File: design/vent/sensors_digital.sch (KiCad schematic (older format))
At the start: 17 parts, among them J12 TEST_1P, J13 TEST_1P, Q1 DMG2302UK, Q2 DMG2302UK, U10 MS5607-02BA03, U6 LP2980AIM5-3.0, U7 LSM6DS3HTR, U8 BMG250, U9 LSM6DS3HTR

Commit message: Add connector part numbers to schematic
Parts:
- C12, C13, C16, C17: footprint Capacitors_SMD:C_0603_HandSoldering -> Capacitors_SMD:C_0805_HandSoldering
- J12, J13: footprint (none) -> TestPoint:TestPoint_Pad_D2.0mm
- Q1, Q2: footprint (none) -> TO_SOT_Packages_SMD:SOT-23_Handsoldering
- R13, R14: footprint (none) -> Resistors_SMD:R_0805_HandSoldering
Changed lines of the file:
@@
 $EndComp
 $Comp
-L GND #PWR61
+L GND #PWR049
 U 1 1 5AE13B89
 P 9100 3150
-F 0 "#PWR61" H 9100 2900 50  0001 C CNN
+F 0 "#PWR049" H 9100 2900 50  0001 C CNN
 F 1 "GND" H 9100 3000 50  0000 C CNN
 F 2 "" H 9100 3150 50  0001 C CNN
@@
 NoConn ~ 9300 1850
 $Comp
-L +3.0V #PWR49
+L +3.0V #PWR050
 U 1 1 5AE13B91
 P 9200 1550
-F 0 "#PWR49" H 9200 1400 50  0001 C CNN
+F 0 "#PWR050" H 9200 1400 50  0001 C CNN
 F 1 "+3.0V" H 9200 1690 50  0000 C CNN
 F 2 "" H 9200 1550 50  0001 C CNN
@@
 F 0 "C12" V 9500 1700 50  0000 L CNN
 F 1 "100nF" V 9500 1350 50  0000 L CNN
-F 2 "Capacitors_SMD:C_0603_HandSoldering" H 9488 1500 50  0001 C CNN
+F 2 "Capacitors_SMD:C_0805_HandSoldering" H 9488 1500 50  0001 C CNN
 F 3 "" H 9450 1650 50  0001 C CNN
 	1    9450 1650
@@
 $EndComp
 $Comp
-L GND #PWR50
+L GND #PWR051
 U 1 1 5AE13B9E
 P 9600 1650
-F 0 "#PWR50" H 9600 1400 50  0001 C CNN
+F 0 "#PWR051" H 9600 1400 50  0001 C CNN
 F 1 "GND" H 9600 1500 50  0000 C CNN
 F 2 "" H 9600 1650 50  0001 C CNN
@@
 $EndComp
 $Comp
-L GND #PWR60
+L GND #PWR052
 U 1 1 5AE13BA4
 P 9950 2800
-F 0 "#PWR60" H 9950 2550 50  0001 C CNN
+F 0 "#PWR052" H 9950 2550 50  0001 C CNN
 F 1 "GND" H 9950 2650 50  0000 C CNN
 F 2 "" H 9950 2800 50  0001 C CNN
@@
 F 0 "C17" H 7050 5200 50  0000 L CNN
 F 1 "100nF" H 6900 5000 50  0000 L CNN
-F 2 "Capacitors_SMD:C_0603_HandSoldering" H 7188 4950 50  0001 C CNN
+F 2 "Capacitors_SMD:C_0805_HandSoldering" H 7188 4950 50  0001 C CNN
 F 3 "" H 7150 5100 50  0001 C CNN
 	1    7150 5100
@@
 $EndComp
 $Comp
-L +3.0V #PWR69
+L +3.0V #PWR053
 U 1 1 5AE13BCB
 P 7150 4700
-F 0 "#PWR69" H 7150 4550 50  0001 C CNN
+F 0 "#PWR053" H 7150 4550 50  0001 C CNN
 F 1 "+3.0V" H 7150 4840 50  0000 C CNN
 F 2 "" H 7150 4700 50  0001 C CNN
@@
 $EndComp
 $Comp
-L GND #PWR72
+L GND #PWR054
 U 1 1 5AE13BD1
 P 7150 5250
-F 0 "#PWR72" H 7150 5000 50  0001 C CNN
+F 0 "#PWR054" H 7150 5000 50  0001 C CNN
 F 1 "GND" H 7150 5100 50  0000 C CNN
 F 2 "" H 7150 5250 50  0001 C CNN
@@
 Barometer/Temperature
 $Comp
-L GND #PWR70
+L GND #PWR055
 U 1 1 5AE13C37
 P 6750 5050
-F 0 "#PWR70" H 6750 4800 50  0001 C CNN
+F 0 "#PWR055" H 6750 4800 50  0001 C CNN
 F 1 "GND" H 6750 4900 50  0000 C CNN
 F 2 "" H 6750 5050 50  0001 C CNN
@@
 SDA_3V
 $Comp
-L +3.0V #PWR55
+L +3.0V #PWR056
 U 1 1 5AE13CB0
 P 8300 2200
-F 0 "#PWR55" H 8300 2050 50  0001 C CNN
+F 0 "#PWR056" H 8300 2050 50  0001 C CNN
 F 1 "+3.0V" H 8300 2340 50  0000 C CNN
 F 2 "" H 8300 2200 50  0001 C CNN
@@
 $EndComp
 $Comp
-L +3.0V #PWR67
+L +3.0V #PWR057
 U 1 1 5AE13CD6
 P 5800 4600
-F 0 "#PWR67" H 5800 4450 50  0001 C CNN
+F 0 "#PWR057" H 5800 4450 50  0001 C CNN
 F 1 "+3.0V" H 5800 4740 50  0000 C CNN
 F 2 "" H 5800 4600 50  0001 C CNN
@@
 $EndComp
 $Comp
-L GND #PWR63
+L GND #PWR058
 U 1 1 5AE13CF8
 P 6150 3550
-F 0 "#PWR63" H 6150 3300 50  0001 C CNN
+F 0 "#PWR058" H 6150 3300 50  0001 C CNN
 F 1 "GND" H 6150 3400 50  0000 C CNN
 F 2 "" H 6150 3550 50  0001 C CNN
@@
 NoConn ~ 6750 3050
 $Comp
-L +3.0V #PWR51
+L +3.0V #PWR059
 U 1 1 5AE13D04
 P 6200 1800
-F 0 "#PWR51" H 6200 1650 50  0001 C CNN
+F 0 "#PWR059" H 6200 1650 50  0001 C CNN
 F 1 "+3.0V" H 6200 1940 50  0000 C CNN
 F 2 "" H 6200 1800 50  0001 C CNN
@@
 F 0 "C13" H 6775 2150 50  0000 L CNN
 F 1 "100nF" H 6775 1950 50  0000 L CNN
-F 2 "Capacitors_SMD:C_0603_HandSoldering" H 6788 1900 50  0001 C CNN
+F 2 "Capacitors_SMD:C_0805_HandSoldering" H 6788 1900 50  0001 C CNN
 F 3 "" H 6750 2050 50  0001 C CNN
 	1    6750 2050
@@
 $EndComp
 $Comp
-L GND #PWR54
+L GND #PWR060
 U 1 1 5AE13D11
 P 6750 2200
-F 0 "#PWR54" H 6750 1950 50  0001 C CNN
+F 0 "#PWR060" H 6750 1950 50  0001 C CNN
 F 1 "GND" H 6750 2050 50  0000 C CNN
 F 2 "" H 6750 2200 50  0001 C CNN
@@
 $EndComp
 $Comp
-L +3.0V #PWR59
+L +3.0V #PWR061
 U 1 1 5AE13D7F
 P 5500 2450
-F 0 "#PWR59" H 5500 2300 50  0001 C CNN
+F 0 "#PWR061" H 5500 2300 50  0001 C CNN
 F 1 "+3.0V" H 5500 2590 50  0000 C CNN
 F 2 "" H 5500 2450 50  0001 C CNN
@@
 F 0 "Q1" H 2450 3950 50  0000 L CNN
 F 1 "DMG2302UK" H 2450 3850 50  0000 L CNN
-F 2 "" H 2450 4000 50  0001 C CNN
+F 2 "TO_SOT_Packages_SMD:SOT-23_Handsoldering" H 2450 4000 50  0001 C CNN
 F 3 "" H 2250 3900 50  0001 C CNN
 	1    2250 3900
@@
 F 0 "R13" V 2830 3750 50  0000 C CNN
 F 1 "10K" V 2750 3750 50  0000 C CNN
-F 2 "" V 2680 3750 50  0001 C CNN
+F 2 "Resistors_SMD:R_0805_HandSoldering" V 2680 3750 50  0001 C CNN
 F 3 "" H 2750 3750 50  0001 C CNN
 	1    2750 3750
@@
 $EndComp
 $Comp
-L +3.0V #PWR62
+L +3.0V #PWR062
 U 1 1 5AE7CAE8
 P 2750 3400
-F 0 "#PWR62" H 2750 3250 50  0001 C CNN
+F 0 "#PWR062" H 2750 3250 50  0001 C CNN
 F 1 "+3.0V" H 2750 3540 50  0000 C CNN
 F 2 "" H 2750 3400 50  0001 C CNN
@@
 F 0 "Q2" H 2450 5250 50  0000 L CNN
 F 1 "DMG2302UK" H 2450 5150 50  0000 L CNN
-F 2 "" H 2450 5300 50  0001 C CNN
+F 2 "TO_SOT_Packages_SMD:SOT-23_Handsoldering" H 2450 5300 50  0001 C CNN
 F 3 "" H 2250 5200 50  0001 C CNN
 	1    2250 5200
@@
 F 0 "R14" V 2830 5050 50  0000 C CNN
 F 1 "10K" V 2750 5050 50  0000 C CNN
-F 2 "" V 2680 5050 50  0001 C CNN
+F 2 "Resistors_SMD:R_0805_HandSoldering" V 2680 5050 50  0001 C CNN
 F 3 "" H 2750 5050 50  0001 C CNN
 	1    2750 5050
@@
 $EndComp
 $Comp
-L +3.0V #PWR68
+L +3.0V #PWR063
 U 1 1 5AE7D3E9
 P 2750 4700
-F 0 "#PWR68" H 2750 4550 50  0001 C CNN
+F 0 "#PWR063" H 2750 4550 50  0001 C CNN
 F 1 "+3.0V" H 2750 4840 50  0000 C CNN
 F 2 "" H 2750 4700 50  0001 C CNN
@@
 $EndComp
 $Comp
-L GND #PWR57
+L GND #PWR064
 U 1 1 5AE808B8
 P 1850 2350
-F 0 "#PWR57" H 1850 2100 50  0001 C CNN
+F 0 "#PWR064" H 1850 2100 50  0001 C CNN
 F 1 "GND" H 1850 2200 50  0000 C CNN
 F 2 "" H 1850 2350 50  0001 C CNN
@@
 $EndComp
 $Comp
-L GND #PWR56
+L GND #PWR065
 U 1 1 5AE808C5
 P 1600 2350
-F 0 "#PWR56" H 1600 2100 50  0001 C CNN
+F 0 "#PWR065" H 1600 2100 50  0001 C CNN
 F 1 "GND" H 1600 2200 50  0000 C CNN
 F 2 "" H 1600 2350 50  0001 C CNN
@@
 $EndComp
 $Comp
-L +3.0V #PWR53
+L +3.0V #PWR066
 U 1 1 5AE808CB
 P 3200 1950
-F 0 "#PWR53" H 3200 1800 50  0001 C CNN
+F 0 "#PWR066" H 3200 1800 50  0001 C CNN
 F 1 "+3.0V" H 3200 2090 50  0000 C CNN
 F 2 "" H 3200 1950 50  0001 C CNN
@@
 $EndComp
 $Comp
-L GND #PWR58
+L GND #PWR067
 U 1 1 5AE808D9
 P 3200 2350
-F 0 "#PWR58" H 3200 2100 50  0001 C CNN
+F 0 "#PWR067" H 3200 2100 50  0001 C CNN
 F 1 "GND" H 3200 2200 50  0000 C CNN
 F 2 "" H 3200 2350 50  0001 C CNN
@@
 Connection ~ 3200 2050
 $Comp
-L +11.1V #PWR52
+L +11.1V #PWR068
 U 1 1 5AE808ED
 P 1600 1950
-F 0 "#PWR52" H 1600 1800 50  0001 C CNN
+F 0 "#PWR068" H 1600 1800 50  0001 C CNN
 F 1 "+11.1V" H 1600 2090 50  0000 C CNN
 F 2 "" H 1600 1950 50  0001 C CNN
@@
 F 0 "J12" H 3250 4120 50  0000 C CNN
 F 1 "TEST_1P" H 3250 4050 50  0000 C CNN
-F 2 "" H 3450 3850 50  0001 C CNN
+F 2 "TestPoint:TestPoint_Pad_D2.0mm" H 3450 3850 50  0001 C CNN
 F 3 "" H 3450 3850 50  0001 C CNN
 	1    3250 3850
@@
 F 0 "J13" H 3250 5420 50  0000 C CNN
 F 1 "TEST_1P" H 3250 5350 50  0000 C CNN
-F 2 "" H 3450 5150 50  0001 C CNN
+F 2 "TestPoint:TestPoint_Pad_D2.0mm" H 3450 5150 50  0001 C CNN
 F 3 "" H 3450 5150 50  0001 C CNN
 	1    3250 5150
@@
 Connection ~ 3250 5300
 $Comp
-L GND #PWR74
+L GND #PWR069
 U 1 1 5AEFCE16
 P 9100 5450
-F 0 "#PWR74" H 9100 5200 50  0001 C CNN
+F 0 "#PWR069" H 9100 5200 50  0001 C CNN
 F 1 "GND" H 9100 5300 50  0000 C CNN
 F 2 "" H 9100 5450 50  0001 C CNN
@@
 NoConn ~ 9300 4150
 $Comp
-L +3.0V #PWR64
+L +3.0V #PWR070
 U 1 1 5AEFCE1E
 P 9200 3850
-F 0 "#PWR64" H 9200 3700 50  0001 C CNN
+F 0 "#PWR070" H 9200 3700 50  0001 C CNN
 F 1 "+3.0V" H 9200 3990 50  0000 C CNN
 F 2 "" H 9200 3850 50  0001 C CNN
@@
 F 0 "C16" V 9500 4000 50  0000 L CNN
 F 1 "100nF" V 9500 3650 50  0000 L CNN
-F 2 "Capacitors_SMD:C_0603_HandSoldering" H 9488 3800 50  0001 C CNN
+F 2 "Capacitors_SMD:C_0805_HandSoldering" H 9488 3800 50  0001 C CNN
 F 3 "" H 9450 3950 50  0001 C CNN
 	1    9450 3950
@@
 $EndComp
 $Comp
-L GND #PWR65
+L GND #PWR071
 U 1 1 5AEFCE2B
 P 9600 3950
-F 0 "#PWR65" H 9600 3700 50  0001 C CNN
+F 0 "#PWR071" H 9600 3700 50  0001 C CNN
 F 1 "GND" H 9600 3800 50  0000 C CNN
 F 2 "" H 9600 3950 50  0001 C CNN
@@
 $EndComp
 $Comp
-L GND #PWR71
+L GND #PWR072
 U 1 1 5AEFCE31
 P 9950 5100
-F 0 "#PWR71" H 9950 4850 50  0001 C CNN
+F 0 "#PWR072" H 9950 4850 50  0001 C CNN
 F 1 "GND" H 9950 4950 50  0000 C CNN
 F 2 "" H 9950 5100 50  0001 C CNN
@@
 SDA_3V
 $Comp
-L +3.0V #PWR73
+L +3.0V #PWR073
 U 1 1 5AEFCE3A
 P 7950 5250
-F 0 "#PWR73" H 7950 5100 50  0001 C CNN
+F 0 "#PWR073" H 7950 5100 50  0001 C CNN
 F 1 "+3.0V" H 7950 5390 50  0000 C CNN
 F 2 "" H 7950 5250 50  0001 C CNN
@@
 	8300 5250 8300 5000
 $Comp
-L GND #PWR66
+L GND #PWR074
 U 1 1 5AF03E59
 P 7950 4450
-F 0 "#PWR66" H 7950 4200 50  0001 C CNN
+F 0 "#PWR074" H 7950 4200 50  0001 C CNN
 F 1 "GND" H 7950 4300 50  0000 C CNN
 F 2 "" H 7950 4450 50  0001 C CNN

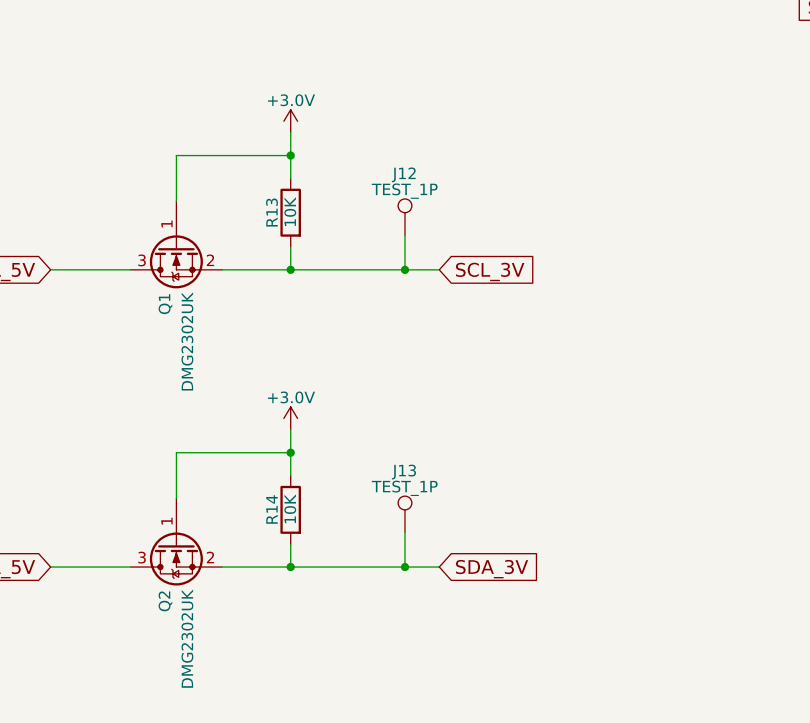
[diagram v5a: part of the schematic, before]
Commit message: Vent & Injector Board Layout
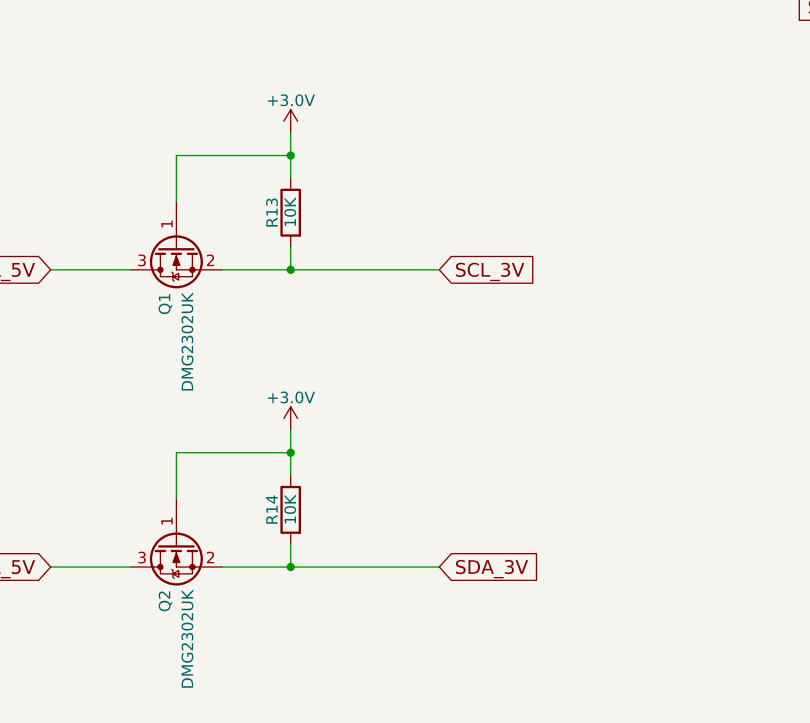
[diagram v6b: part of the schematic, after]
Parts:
- removed J12, J13: TEST_1P, TestPoint:TestPoint_Pad_D2.0mm, symbol TEST_1P
- U10: footprint footprints:MS560702BA03 -> Flight_Instr:MS560702BA03
- U7, U9: footprint LSM6DS3:PQFN50P300X250X86-14N -> Flight_Instr:LSM6DS3HTR
- U8: footprint footprints:Bosch_LGA-14 -> Flight_Instr:Bosch_LGA-14
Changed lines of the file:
@@
 F 0 "U10" H 6100 5750 60  0000 C CNN
 F 1 "MS5607-02BA03" H 6350 5200 60  0000 C CNN
-F 2 "footprints:MS560702BA03" H 6350 5200 60  0001 C CNN
+F 2 "Flight_Instr:MS560702BA03" H 6350 5200 60  0001 C CNN
 F 3 "" H 6350 5200 60  0001 C CNN
 	1    6300 5200
@@
 $EndComp
 $Comp
-L GND #PWR047
+L GND #PWR045
 U 1 1 5AE13B89
 P 9100 3150
-F 0 "#PWR047" H 9100 2900 50  0001 C CNN
+F 0 "#PWR045" H 9100 2900 50  0001 C CNN
 F 1 "GND" H 9100 3000 50  0000 C CNN
 F 2 "" H 9100 3150 50  0001 C CNN
@@
 NoConn ~ 9300 1850
 $Comp
-L +3.0V #PWR048
+L +3.0V #PWR046
 U 1 1 5AE13B91
 P 9200 1550
-F 0 "#PWR048" H 9200 1400 50  0001 C CNN
+F 0 "#PWR046" H 9200 1400 50  0001 C CNN
 F 1 "+3.0V" H 9200 1690 50  0000 C CNN
 F 2 "" H 9200 1550 50  0001 C CNN
@@
 $EndComp
 $Comp
-L GND #PWR049
+L GND #PWR047
 U 1 1 5AE13B9E
 P 9600 1650
-F 0 "#PWR049" H 9600 1400 50  0001 C CNN
+F 0 "#PWR047" H 9600 1400 50  0001 C CNN
 F 1 "GND" H 9600 1500 50  0000 C CNN
 F 2 "" H 9600 1650 50  0001 C CNN
@@
 $EndComp
 $Comp
-L GND #PWR050
+L GND #PWR048
 U 1 1 5AE13BA4
 P 9950 2800
-F 0 "#PWR050" H 9950 2550 50  0001 C CNN
+F 0 "#PWR048" H 9950 2550 50  0001 C CNN
 F 1 "GND" H 9950 2650 50  0000 C CNN
 F 2 "" H 9950 2800 50  0001 C CNN
@@
 $EndComp
 $Comp
-L +3.0V #PWR051
+L +3.0V #PWR049
 U 1 1 5AE13BCB
 P 7150 4700
-F 0 "#PWR051" H 7150 4550 50  0001 C CNN
+F 0 "#PWR049" H 7150 4550 50  0001 C CNN
 F 1 "+3.0V" H 7150 4840 50  0000 C CNN
 F 2 "" H 7150 4700 50  0001 C CNN
@@
 $EndComp
 $Comp
-L GND #PWR052
+L GND #PWR050
 U 1 1 5AE13BD1
 P 7150 5250
-F 0 "#PWR052" H 7150 5000 50  0001 C CNN
+F 0 "#PWR050" H 7150 5000 50  0001 C CNN
 F 1 "GND" H 7150 5100 50  0000 C CNN
 F 2 "" H 7150 5250 50  0001 C CNN
@@
 Barometer/Temperature
 $Comp
-L GND #PWR053
+L GND #PWR051
 U 1 1 5AE13C37
 P 6750 5050
-F 0 "#PWR053" H 6750 4800 50  0001 C CNN
+F 0 "#PWR051" H 6750 4800 50  0001 C CNN
 F 1 "GND" H 6750 4900 50  0000 C CNN
 F 2 "" H 6750 5050 50  0001 C CNN
@@
 SDA_3V
 $Comp
-L +3.0V #PWR054
+L +3.0V #PWR052
 U 1 1 5AE13CB0
 P 8300 2200
-F 0 "#PWR054" H 8300 2050 50  0001 C CNN
+F 0 "#PWR052" H 8300 2050 50  0001 C CNN
 F 1 "+3.0V" H 8300 2340 50  0000 C CNN
 F 2 "" H 8300 2200 50  0001 C CNN
@@
 $EndComp
 $Comp
-L +3.0V #PWR055
+L +3.0V #PWR053
 U 1 1 5AE13CD6
 P 5800 4600
-F 0 "#PWR055" H 5800 4450 50  0001 C CNN
+F 0 "#PWR053" H 5800 4450 50  0001 C CNN
 F 1 "+3.0V" H 5800 4740 50  0000 C CNN
 F 2 "" H 5800 4600 50  0001 C CNN
@@
 $EndComp
 $Comp
-L GND #PWR056
+L GND #PWR054
 U 1 1 5AE13CF8
 P 6150 3550
-F 0 "#PWR056" H 6150 3300 50  0001 C CNN
+F 0 "#PWR054" H 6150 3300 50  0001 C CNN
 F 1 "GND" H 6150 3400 50  0000 C CNN
 F 2 "" H 6150 3550 50  0001 C CNN
@@
 NoConn ~ 6750 3050
 $Comp
-L +3.0V #PWR057
+L +3.0V #PWR055
 U 1 1 5AE13D04
 P 6200 1800
-F 0 "#PWR057" H 6200 1650 50  0001 C CNN
+F 0 "#PWR055" H 6200 1650 50  0001 C CNN
 F 1 "+3.0V" H 6200 1940 50  0000 C CNN
 F 2 "" H 6200 1800 50  0001 C CNN
@@
 $EndComp
 $Comp
-L GND #PWR058
+L GND #PWR056
 U 1 1 5AE13D11
 P 6750 2200
-F 0 "#PWR058" H 6750 1950 50  0001 C CNN
+F 0 "#PWR056" H 6750 1950 50  0001 C CNN
 F 1 "GND" H 6750 2050 50  0000 C CNN
 F 2 "" H 6750 2200 50  0001 C CNN
@@
 $EndComp
 $Comp
-L +3.0V #PWR059
+L +3.0V #PWR057
 U 1 1 5AE13D7F
 P 5500 2450
-F 0 "#PWR059" H 5500 2300 50  0001 C CNN
+F 0 "#PWR057" H 5500 2300 50  0001 C CNN
 F 1 "+3.0V" H 5500 2590 50  0000 C CNN
 F 2 "" H 5500 2450 50  0001 C CNN
@@
 F 0 "U8" H 5950 3700 60  0000 C CNN
 F 1 "BMG250" H 6450 2650 60  0000 C CNN
-F 2 "footprints:Bosch_LGA-14" H 6150 2950 60  0001 C CNN
+F 2 "Flight_Instr:Bosch_LGA-14" H 6150 2950 60  0001 C CNN
 F 3 "" H 6150 2950 60  0001 C CNN
 	1    6250 2950
@@
 F 0 "U7" H 8800 3150 60  0000 C CNN
 F 1 "LSM6DS3HTR" H 9650 2000 60  0000 C CNN
-F 2 "LSM6DS3:PQFN50P300X250X86-14N" H 9100 2300 60  0001 C CNN
+F 2 "Flight_Instr:LSM6DS3HTR" H 9100 2300 60  0001 C CNN
 F 3 "" H 9100 2300 60  0001 C CNN
 	1    9200 2550
@@
 $EndComp
 $Comp
-L +3.0V #PWR060
+L +3.0V #PWR058
 U 1 1 5AE7CAE8
 P 2750 3400
-F 0 "#PWR060" H 2750 3250 50  0001 C CNN
+F 0 "#PWR058" H 2750 3250 50  0001 C CNN
 F 1 "+3.0V" H 2750 3540 50  0000 C CNN
 F 2 "" H 2750 3400 50  0001 C CNN
@@
 $EndComp
 $Comp
-L +3.0V #PWR061
+L +3.0V #PWR059
 U 1 1 5AE7D3E9
 P 2750 4700
-F 0 "#PWR061" H 2750 4550 50  0001 C CNN
+F 0 "#PWR059" H 2750 4550 50  0001 C CNN
 F 1 "+3.0V" H 2750 4840 50  0000 C CNN
 F 2 "" H 2750 4700 50  0001 C CNN
@@
 $EndComp
 $Comp
-L GND #PWR062
+L GND #PWR060
 U 1 1 5AE808B8
 P 1850 2350
-F 0 "#PWR062" H 1850 2100 50  0001 C CNN
+F 0 "#PWR060" H 1850 2100 50  0001 C CNN
 F 1 "GND" H 1850 2200 50  0000 C CNN
 F 2 "" H 1850 2350 50  0001 C CNN
@@
 $EndComp
 $Comp
-L GND #PWR063
+L GND #PWR061
 U 1 1 5AE808C5
 P 1600 2350
-F 0 "#PWR063" H 1600 2100 50  0001 C CNN
+F 0 "#PWR061" H 1600 2100 50  0001 C CNN
 F 1 "GND" H 1600 2200 50  0000 C CNN
 F 2 "" H 1600 2350 50  0001 C CNN
@@
 $EndComp
 $Comp
-L +3.0V #PWR064
+L +3.0V #PWR062
 U 1 1 5AE808CB
 P 3200 1950
-F 0 "#PWR064" H 3200 1800 50  0001 C CNN
+F 0 "#PWR062" H 3200 1800 50  0001 C CNN
 F 1 "+3.0V" H 3200 2090 50  0000 C CNN
 F 2 "" H 3200 1950 50  0001 C CNN
@@
 $EndComp
 $Comp
-L GND #PWR065
+L GND #PWR063
 U 1 1 5AE808D9
 P 3200 2350
-F 0 "#PWR065" H 3200 2100 50  0001 C CNN
+F 0 "#PWR063" H 3200 2100 50  0001 C CNN
 F 1 "GND" H 3200 2200 50  0000 C CNN
 F 2 "" H 3200 2350 50  0001 C CNN
@@
 Connection ~ 3200 2050
 $Comp
-L +11.1V #PWR066
+L +11.1V #PWR064
 U 1 1 5AE808ED
 P 1600 1950
-F 0 "#PWR066" H 1600 1800 50  0001 C CNN
+F 0 "#PWR064" H 1600 1800 50  0001 C CNN
 F 1 "+11.1V" H 1600 2090 50  0000 C CNN
 F 2 "" H 1600 1950 50  0001 C CNN
@@
 $EndComp
 $Comp
-L TEST_1P J12
-U 1 1 5AEBBCFA
-P 3250 3850
-F 0 "J12" H 3250 4120 50  0000 C CNN
-F 1 "TEST_1P" H 3250 4050 50  0000 C CNN
-F 2 "TestPoint:TestPoint_Pad_D2.0mm" H 3450 3850 50  0001 C CNN
-F 3 "" H 3450 3850 50  0001 C CNN
-	1    3250 3850
-	1    0    0    -1
-$EndComp
-$Comp
-L TEST_1P J13
-U 1 1 5AEBBD4E
-P 3250 5150
-F 0 "J13" H 3250 5420 50  0000 C CNN
-F 1 "TEST_1P" H 3250 5350 50  0000 C CNN
-F 2 "TestPoint:TestPoint_Pad_D2.0mm" H 3450 5150 50  0001 C CNN
-F 3 "" H 3450 5150 50  0001 C CNN
-	1    3250 5150
-	1    0    0    -1
-$EndComp
-Wire Wire Line
-	3250 3850 3250 4000
-Connection ~ 3250 4000
-Wire Wire Line
-	3250 5150 3250 5300
-Connection ~ 3250 5300
-$Comp
-L GND #PWR067
+L GND #PWR065
 U 1 1 5AEFCE16
 P 9100 5450
-F 0 "#PWR067" H 9100 5200 50  0001 C CNN
+F 0 "#PWR065" H 9100 5200 50  0001 C CNN
 F 1 "GND" H 9100 5300 50  0000 C CNN
 F 2 "" H 9100 5450 50  0001 C CNN
@@
 NoConn ~ 9300 4150
 $Comp
-L +3.0V #PWR068
+L +3.0V #PWR066
 U 1 1 5AEFCE1E
 P 9200 3850
-F 0 "#PWR068" H 9200 3700 50  0001 C CNN
+F 0 "#PWR066" H 9200 3700 50  0001 C CNN
 F 1 "+3.0V" H 9200 3990 50  0000 C CNN
 F 2 "" H 9200 3850 50  0001 C CNN
@@
 $EndComp
 $Comp
-L GND #PWR069
+L GND #PWR067
 U 1 1 5AEFCE2B
 P 9600 3950
-F 0 "#PWR069" H 9600 3700 50  0001 C CNN
+F 0 "#PWR067" H 9600 3700 50  0001 C CNN
 F 1 "GND" H 9600 3800 50  0000 C CNN
 F 2 "" H 9600 3950 50  0001 C CNN
@@
 $EndComp
 $Comp
-L GND #PWR070
+L GND #PWR068
 U 1 1 5AEFCE31
 P 9950 5100
-F 0 "#PWR070" H 9950 4850 50  0001 C CNN
+F 0 "#PWR068" H 9950 4850 50  0001 C CNN
 F 1 "GND" H 9950 4950 50  0000 C CNN
 F 2 "" H 9950 5100 50  0001 C CNN
@@
 SDA_3V
 $Comp
-L +3.0V #PWR071
+L +3.0V #PWR069
 U 1 1 5AEFCE3A
 P 7950 5250
-F 0 "#PWR071" H 7950 5100 50  0001 C CNN
+F 0 "#PWR069" H 7950 5100 50  0001 C CNN
 F 1 "+3.0V" H 7950 5390 50  0000 C CNN
 F 2 "" H 7950 5250 50  0001 C CNN
@@
 F 0 "U9" H 8800 5450 60  0000 C CNN
 F 1 "LSM6DS3HTR" H 9650 4300 60  0000 C CNN
-F 2 "LSM6DS3:PQFN50P300X250X86-14N" H 9100 4600 60  0001 C CNN
+F 2 "Flight_Instr:LSM6DS3HTR" H 9100 4600 60  0001 C CNN
 F 3 "" H 9100 4600 60  0001 C CNN
 	1    9200 4850
@@
 	8300 5250 8300 5000
 $Comp
-L GND #PWR072
+L GND #PWR070
 U 1 1 5AF03E59
 P 7950 4450
-F 0 "#PWR072" H 7950 4200 50  0001 C CNN
+F 0 "#PWR070" H 7950 4200 50  0001 C CNN
 F 1 "GND" H 7950 4300 50  0000 C CNN
 F 2 "" H 7950 4450 50  0001 C CNN
